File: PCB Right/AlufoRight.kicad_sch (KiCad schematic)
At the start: 32 parts, among them J10 Shield_Connection, J2 USB_C_Receptacle_USB2.0_16P_2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, J4 USB_C_Receptacle_USB2.0_16P_2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, J6 Shield_Connection, J8 Shield_Connection, SW2 BOOT, U2 CH552T, U4 USBLC6-2P6, U6 USBLC6-2P6

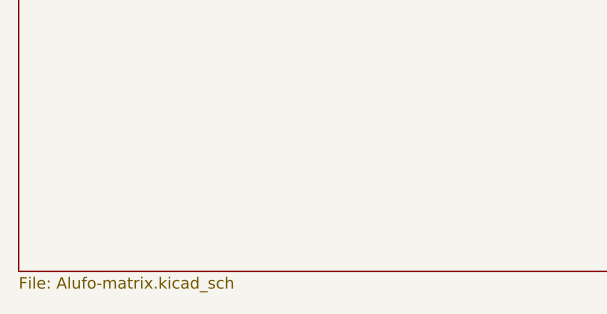
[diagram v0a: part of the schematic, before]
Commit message: Rename righthand PCB project internally
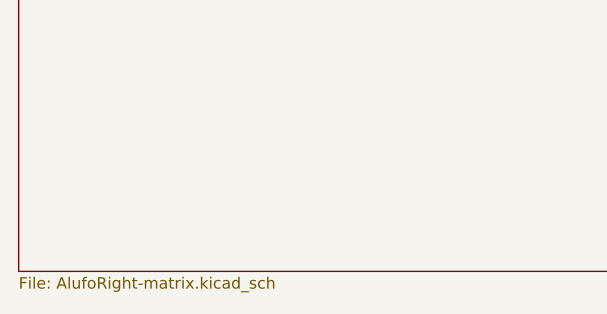
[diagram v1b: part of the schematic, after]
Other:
- sheet Matrix: file Alufo-matrix.kicad_sch -> AlufoRight-matrix.kicad_sch
- title: Alufo  -> Alufo
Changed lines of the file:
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@@
 	(paper "A4" portrait)
 	(title_block
-		(title "Alufo ")
+		(title "Alufo")
 		(rev "1.1R")
 		(company "bgkendall")
@@
 		)
 		(instances
-			(project "Alufo"
+			(project "AlufoRight"
 				(path "/52f043ac-ccff-4c85-bc10-2db9d3c9e3f3"
 					(reference "J2")
@@
 		)
 		(instances
-			(project "Alufo"
+			(project "AlufoRight"
 				(path "/52f043ac-ccff-4c85-bc10-2db9d3c9e3f3"
 					(reference "H12")
@@
 		)
 		(instances
-			(project "Alufo"
+			(project "AlufoRight"
 				(path "/52f043ac-ccff-4c85-bc10-2db9d3c9e3f3"
 					(reference "J4")
@@
 		)
 		(instances
-			(project "Alufo"
+			(project "AlufoRight"
 				(path "/52f043ac-ccff-4c85-bc10-2db9d3c9e3f3"
 					(reference "U6")
@@
 		)
 		(instances
-			(project "Alufo"
+			(project "AlufoRight"
 				(path "/52f043ac-ccff-4c85-bc10-2db9d3c9e3f3"
 					(reference "J8")
@@
 		)
 		(instances
-			(project "Alufo"
+			(project "AlufoRight"
 				(path "/52f043ac-ccff-4c85-bc10-2db9d3c9e3f3"
 					(reference "C2")
@@
 		)
 		(instances
-			(project "Alufo"
+			(project "AlufoRight"
 				(path "/52f043ac-ccff-4c85-bc10-2db9d3c9e3f3"
 					(reference "H14")
@@
 		)
 		(instances
-			(project "Alufo"
+			(project "AlufoRight"
 				(path "/52f043ac-ccff-4c85-bc10-2db9d3c9e3f3"
 					(reference "#PWR030")
@@
 		)
 		(instances
-			(project "Alufo"
+			(project "AlufoRight"
 				(path "/52f043ac-ccff-4c85-bc10-2db9d3c9e3f3"
 					(reference "#PWR032")
@@
 		)
 		(instances
-			(project "Alufo"
+			(project "AlufoRight"
 				(path "/52f043ac-ccff-4c85-bc10-2db9d3c9e3f3"
 					(reference "H5")
@@
 		)
 		(instances
-			(project "Alufo"
+			(project "AlufoRight"
 				(path "/52f043ac-ccff-4c85-bc10-2db9d3c9e3f3"
 					(reference "#PWR035")
@@
 		)
 		(instances
-			(project "Alufo"
+			(project "AlufoRight"
 				(path "/52f043ac-ccff-4c85-bc10-2db9d3c9e3f3"
 					(reference "#PWR026")
@@
 		)
 		(instances
-			(project "Alufo"
+			(project "AlufoRight"
 				(path "/52f043ac-ccff-4c85-bc10-2db9d3c9e3f3"
 					(reference "J10")
@@
 		)
 		(instances
-			(project "Alufo"
+			(project "AlufoRight"
 				(path "/52f043ac-ccff-4c85-bc10-2db9d3c9e3f3"
 					(reference "H11")
@@
 		)
 		(instances
-			(project "Alufo"
+			(project "AlufoRight"
 				(path "/52f043ac-ccff-4c85-bc10-2db9d3c9e3f3"
 					(reference "#PWR033")
@@
 		)
 		(instances
-			(project "Alufo"
+			(project "AlufoRight"
 				(path "/52f043ac-ccff-4c85-bc10-2db9d3c9e3f3"
 					(reference "H8")
@@
 		)
 		(instances
-			(project "Alufo"
+			(project "AlufoRight"
 				(path "/52f043ac-ccff-4c85-bc10-2db9d3c9e3f3"
 					(reference "C4")
@@
 		)
 		(instances
-			(project "Alufo"
+			(project "AlufoRight"
 				(path "/52f043ac-ccff-4c85-bc10-2db9d3c9e3f3"
 					(reference "#PWR029")
@@
 		)
 		(instances
-			(project "Alufo"
+			(project "AlufoRight"
 				(path "/52f043ac-ccff-4c85-bc10-2db9d3c9e3f3"
 					(reference "R2")
@@
 		)
 		(instances
-			(project "Alufo"
+			(project "AlufoRight"
 				(path "/52f043ac-ccff-4c85-bc10-2db9d3c9e3f3"
 					(reference "#PWR031")
@@
 		)
 		(instances
-			(project "Alufo"
+			(project "AlufoRight"
 				(path "/52f043ac-ccff-4c85-bc10-2db9d3c9e3f3"
 					(reference "#PWR010")
@@
 		)
 		(instances
-			(project "Alufo"
+			(project "AlufoRight"
 				(path "/52f043ac-ccff-4c85-bc10-2db9d3c9e3f3"
 					(reference "F2")
@@
 		)
 		(instances
-			(project "Alufo"
+			(project "AlufoRight"
 				(path "/52f043ac-ccff-4c85-bc10-2db9d3c9e3f3"
 					(reference "H1")
@@
 		)
 		(instances
-			(project "Alufo"
+			(project "AlufoRight"
 				(path "/52f043ac-ccff-4c85-bc10-2db9d3c9e3f3"
 					(reference "#PWR023")
@@
 		)
 		(instances
-			(project "Alufo"
+			(project "AlufoRight"
 				(path "/52f043ac-ccff-4c85-bc10-2db9d3c9e3f3"
 					(reference "#PWR036")
@@
 		)
 		(instances
-			(project "Alufo"
+			(project "AlufoRight"
 				(path "/52f043ac-ccff-4c85-bc10-2db9d3c9e3f3"
 					(reference "#PWR034")
@@
 		)
 		(instances
-			(project "Alufo"
+			(project "AlufoRight"
 				(path "/52f043ac-ccff-4c85-bc10-2db9d3c9e3f3"
 					(reference "H7")
@@
 		)
 		(instances
-			(project "Alufo"
+			(project "AlufoRight"
 				(path "/52f043ac-ccff-4c85-bc10-2db9d3c9e3f3"
 					(reference "H4")
@@
 		)
 		(instances
-			(project "Alufo"
+			(project "AlufoRight"
 				(path "/52f043ac-ccff-4c85-bc10-2db9d3c9e3f3"
 					(reference "H13")
@@
 		)
 		(instances
-			(project "Alufo"
+			(project "AlufoRight"
 				(path "/52f043ac-ccff-4c85-bc10-2db9d3c9e3f3"
 					(reference "#PWR020")
@@
 		)
 		(instances
-			(project "Alufo"
+			(project "AlufoRight"
 				(path "/52f043ac-ccff-4c85-bc10-2db9d3c9e3f3"
 					(reference "#PWR028")
@@
 		)
 		(instances
-			(project "Alufo"
+			(project "AlufoRight"
 				(path "/52f043ac-ccff-4c85-bc10-2db9d3c9e3f3"
 					(reference "R4")
@@
 		)
 		(instances
-			(project "Alufo"
+			(project "AlufoRight"
 				(path "/52f043ac-ccff-4c85-bc10-2db9d3c9e3f3"
 					(reference "U4")
@@
 		)
 		(instances
-			(project "Alufo"
+			(project "AlufoRight"
 				(path "/52f043ac-ccff-4c85-bc10-2db9d3c9e3f3"
 					(reference "#PWR021")
@@
 		)
 		(instances
-			(project "Alufo"
+			(project "AlufoRight"
 				(path "/52f043ac-ccff-4c85-bc10-2db9d3c9e3f3"
 					(reference "#PWR022")
@@
 		)
 		(instances
-			(project "Alufo"
+			(project "AlufoRight"
 				(path "/52f043ac-ccff-4c85-bc10-2db9d3c9e3f3"
 					(reference "#PWR025")
@@
 		)
 		(instances
-			(project "Alufo"
+			(project "AlufoRight"
 				(path "/52f043ac-ccff-4c85-bc10-2db9d3c9e3f3"
 					(reference "H10")
@@
 		)
 		(instances
-			(project "Alufo"
+			(project "AlufoRight"
 				(path "/52f043ac-ccff-4c85-bc10-2db9d3c9e3f3"
 					(reference "#PWR027")
@@
 		)
 		(instances
-			(project "Alufo"
+			(project "AlufoRight"
 				(path "/52f043ac-ccff-4c85-bc10-2db9d3c9e3f3"
 					(reference "#PWR024")
@@
 		)
 		(instances
-			(project "Alufo"
+			(project "AlufoRight"
 				(path "/52f043ac-ccff-4c85-bc10-2db9d3c9e3f3"
 					(reference "H3")
@@
 		)
 		(instances
-			(project "Alufo"
+			(project "AlufoRight"
 				(path "/52f043ac-ccff-4c85-bc10-2db9d3c9e3f3"
 					(reference "R6")
@@
 		)
 		(instances
-			(project "Alufo"
+			(project "AlufoRight"
 				(path "/52f043ac-ccff-4c85-bc10-2db9d3c9e3f3"
 					(reference "H9")
@@
 		)
 		(instances
-			(project "Alufo"
+			(project "AlufoRight"
 				(path "/52f043ac-ccff-4c85-bc10-2db9d3c9e3f3"
 					(reference "#PWR037")
@@
 		)
 		(instances
-			(project "Alufo"
+			(project "AlufoRight"
 				(path "/52f043ac-ccff-4c85-bc10-2db9d3c9e3f3"
 					(reference "R8")
@@
 		)
 		(instances
-			(project "Alufo"
+			(project "AlufoRight"
 				(path "/52f043ac-ccff-4c85-bc10-2db9d3c9e3f3"
 					(reference "SW2")
@@
 		)
 		(instances
-			(project "Alufo"
+			(project "AlufoRight"
 				(path "/52f043ac-ccff-4c85-bc10-2db9d3c9e3f3"
 					(reference "H6")
@@
 		)
 		(instances
-			(project "Alufo"
+			(project "AlufoRight"
 				(path "/52f043ac-ccff-4c85-bc10-2db9d3c9e3f3"
 					(reference "D2")
@@
 		)
 		(instances
-			(project "Alufo"
+			(project "AlufoRight"
 				(path "/52f043ac-ccff-4c85-bc10-2db9d3c9e3f3"
 					(reference "H2")
@@
 		)
 		(instances
-			(project "Alufo"
+			(project "AlufoRight"
 				(path "/52f043ac-ccff-4c85-bc10-2db9d3c9e3f3"
 					(reference "J6")
@@
 			)
 		)
-		(property "Sheetfile" "Alufo-matrix.kicad_sch"
+		(property "Sheetfile" "AlufoRight-matrix.kicad_sch"
 			(at 15.24 250.7746 0)
 			(effects
@@
 		)
 		(instances
-			(project "Alufo"
+			(project "AlufoRight"
 				(path "/52f043ac-ccff-4c85-bc10-2db9d3c9e3f3"
 					(page "2")

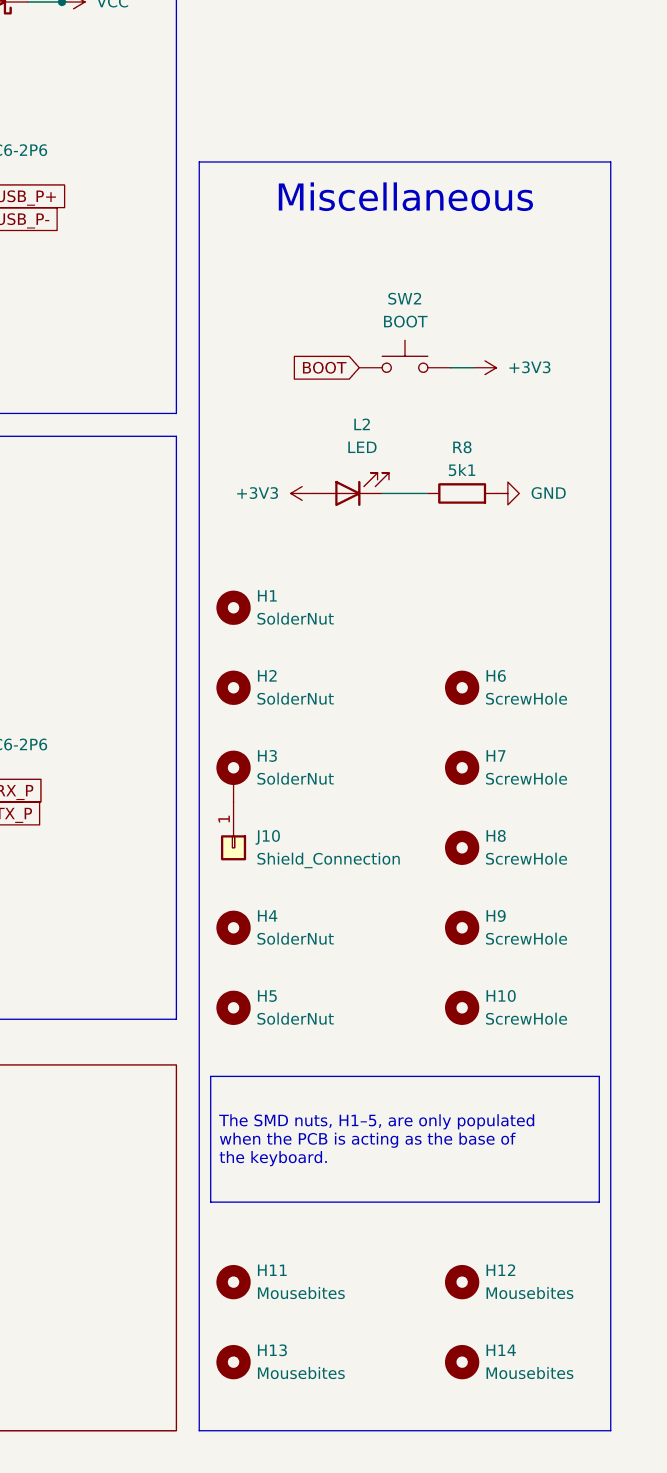
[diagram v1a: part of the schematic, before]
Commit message: Remove plate from left and right PCBs
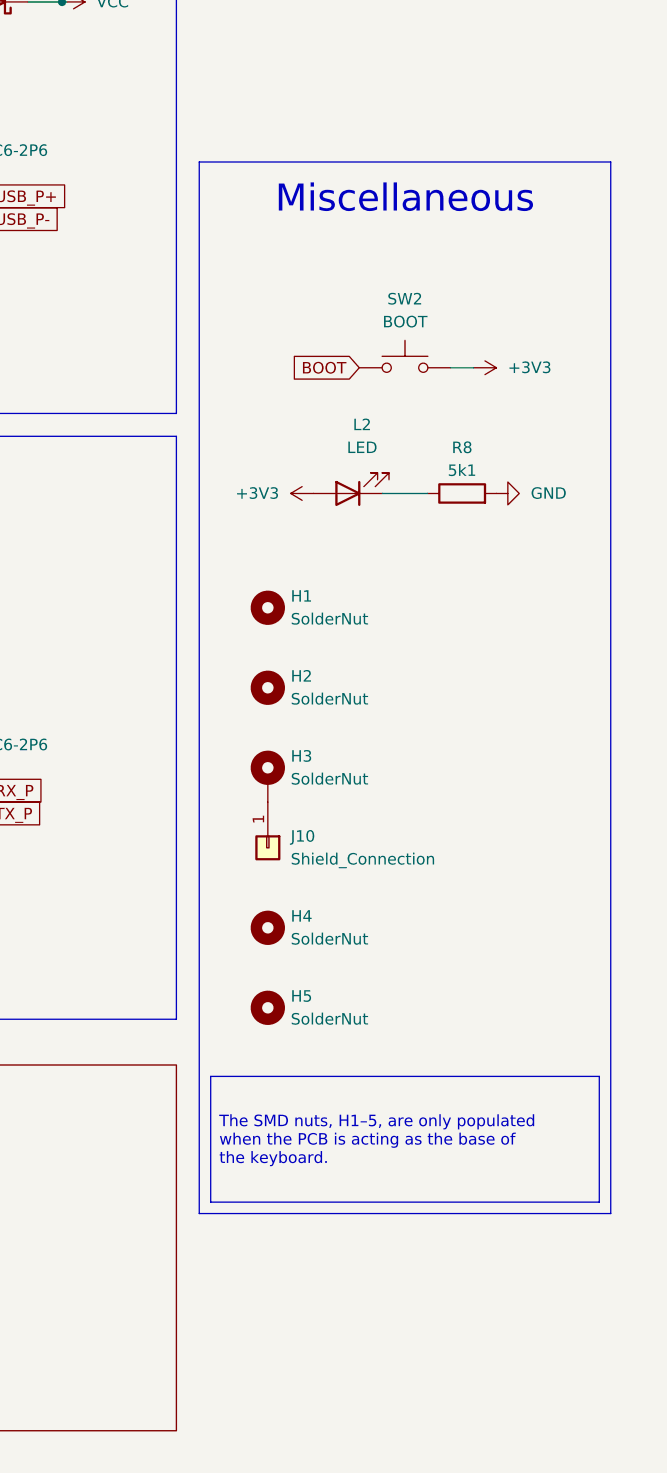
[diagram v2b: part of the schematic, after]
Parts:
- removed H10, H6, H7, H8, H9: ScrewHole, MountingHole:MountingHole_2.2mm_M2, symbol Mechanical:MountingHole
- removed H11, H12, H13, H14: Mousebites, Project_Library:Mousebites, symbol Mechanical:MountingHole
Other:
- moved on the sheet: H1, H2, H3, H4, H5, J10
